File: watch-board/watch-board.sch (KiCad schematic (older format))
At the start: 60 parts

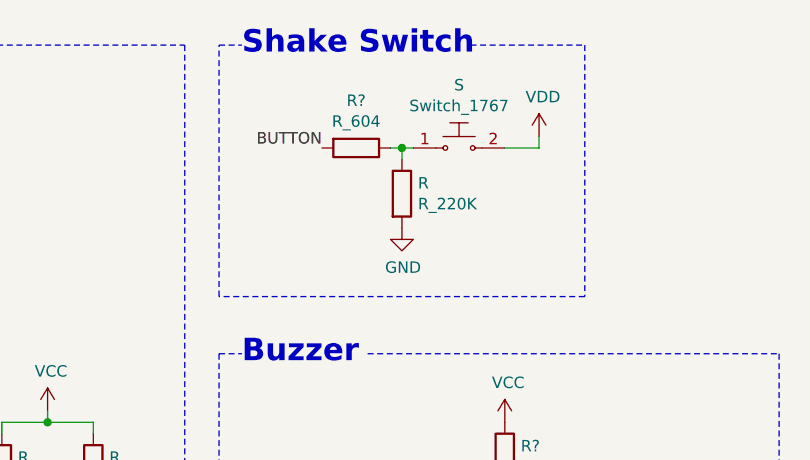
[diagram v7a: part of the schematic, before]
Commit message: Confirming shake-switch circuit -- adjusting pull-down and current limiting resistor
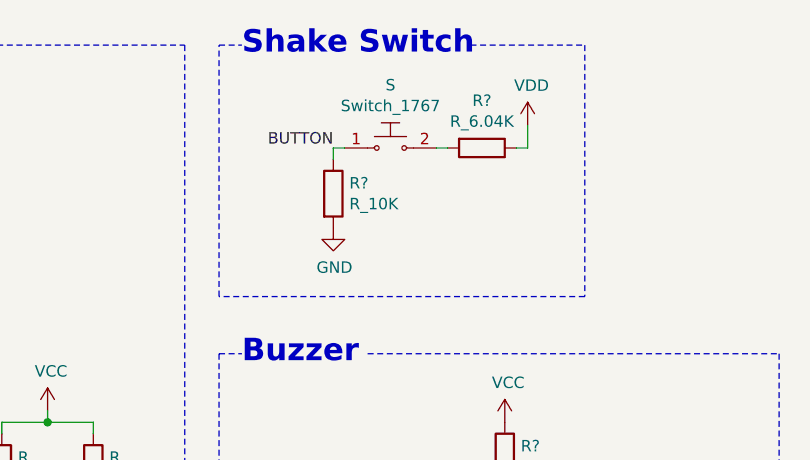
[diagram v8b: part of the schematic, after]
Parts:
- removed R: R_220K, Resistor_SMD:R_0805_2012Metric, symbol luke:R_220K
- removed R?: R_604, Resistor_SMD:R_0805_2012Metric, symbol luke:R_604
- added R?: R_6.04K, Resistor_SMD:R_0805_2012Metric, symbol luke:R_6.04K
- added R?: R_10K, Resistor_SMD:R_0805_2012Metric, symbol luke:R_10K
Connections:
- net BUTTON: now also S.1, R?.1
- net GND: now also R?.2
- net VDD: now also R?.1; no longer S.2
- new net: R?.2, S.2
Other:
- moved on the sheet: S
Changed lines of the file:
@@
 L luke:Switch_1767 S
 U 1 1 5F0E6B9E
-P 6850 1150
-F 0 "S" H 6850 1425 50  0000 C CNN
-F 1 "Switch_1767" H 6850 1334 50  0000 C CNN
-F 2 "Connector_PinSocket_2.54mm:PinSocket_1x02_P2.54mm_Vertical" H 7050 1350 50  0001 L CNN
-F 3 "https://media.digikey.com/pdf/Data%20Sheets/Adafruit%20PDFs/1767_Web.pdf" H 7050 1450 60  0001 L CNN
-F 4 "1528-2159-ND" H 7050 1550 60  0001 L CNN "Digi-Key_PN"
-F 5 "https://www.digikey.com/product-detail/en/adafruit-industries-llc/1767/1528-2159-ND/7244945" H 7050 1450 50  0001 L CNN "Purchasing Link"
-	1    6850 1150
-	1    0    0    -1
-$EndComp
-Text Label 6250 1150 2    50   ~ 0
+P 6550 1150
+F 0 "S" H 6550 1425 50  0000 C CNN
+F 1 "Switch_1767" H 6550 1334 50  0000 C CNN
+F 2 "Connector_PinSocket_2.54mm:PinSocket_1x02_P2.54mm_Vertical" H 6750 1350 50  0001 L CNN
+F 3 "https://media.digikey.com/pdf/Data%20Sheets/Adafruit%20PDFs/1767_Web.pdf" H 6750 1450 60  0001 L CNN
+F 4 "1528-2159-ND" H 6750 1550 60  0001 L CNN "Digi-Key_PN"
+F 5 "https://www.digikey.com/product-detail/en/adafruit-industries-llc/1767/1528-2159-ND/7244945" H 6750 1450 50  0001 L CNN "Purchasing Link"
+	1    6550 1150
+	1    0    0    -1
+$EndComp
+Text Label 6300 1150 2    50   ~ 0
 BUTTON
 Wire Wire Line
-	6550 1150 6600 1150
-$Comp
-L luke:R_220K R
-U 1 1 5ED88523
-P 6600 1350
-F 0 "R" H 6670 1396 50  0000 L CNN
-F 1 "R_220K" H 6670 1305 50  0000 L CNN
-F 2 "Resistor_SMD:R_0805_2012Metric" H 5500 1650 50  0001 L CNN
-F 3 "https://www.te.com/commerce/DocumentDelivery/DDEController?Action=srchrtrv&DocNm=1773204&DocType=DS&DocLang=English" H 5500 1750 50  0001 L CNN
-F 4 "A126350CT-ND" H 5500 1550 60  0001 L CNN "Digi-Key_PN"
-F 5 "https://www.digikey.com/product-detail/en/te-connectivity-passive-product/CRG0805F220K/A126350CT-ND/7603405" H 5500 1850 60  0001 L CNN "Purchasing Link"
-	1    6600 1350
-	1    0    0    -1
-$EndComp
-Wire Wire Line
-	6600 1200 6600 1150
-Connection ~ 6600 1150
-Wire Wire Line
-	6600 1150 6650 1150
+	6300 1200 6300 1150
 $Comp
 L power:GND #PWR
 U 1 1 5ED90D9E
-P 6600 1500
-F 0 "#PWR" H 6600 1250 50  0001 C CNN
-F 1 "GND" H 6605 1327 50  0000 C CNN
-F 2 "" H 6600 1500 50  0001 C CNN
-F 3 "" H 6600 1500 50  0001 C CNN
-	1    6600 1500
+P 6300 1500
+F 0 "#PWR" H 6300 1250 50  0001 C CNN
+F 1 "GND" H 6305 1327 50  0000 C CNN
+F 2 "" H 6300 1500 50  0001 C CNN
+F 3 "" H 6300 1500 50  0001 C CNN
+	1    6300 1500
 	1    0    0    -1
 $EndComp
@@
 L power:VDD #PWR
 U 1 1 5F1738F3
-P 7200 1100
-F 0 "#PWR" H 7200 950 50  0001 C CNN
-F 1 "VDD" H 7217 1273 50  0000 C CNN
-F 2 "" H 7200 1100 50  0001 C CNN
-F 3 "" H 7200 1100 50  0001 C CNN
-	1    7200 1100
-	1    0    0    -1
-$EndComp
-Wire Wire Line
-	7050 1150 7200 1150
-Wire Wire Line
-	7200 1150 7200 1100
+P 7150 1050
+F 0 "#PWR" H 7150 900 50  0001 C CNN
+F 1 "VDD" H 7167 1223 50  0000 C CNN
+F 2 "" H 7150 1050 50  0001 C CNN
+F 3 "" H 7150 1050 50  0001 C CNN
+	1    7150 1050
+	1    0    0    -1
+$EndComp
 Text Label 4850 5950 0    50   ~ 0
 VBAT_OK
@@
 	0    1    1    0
 $EndComp
-$Comp
-L luke:R_604 R?
-U 1 1 5FA72838
-P 6400 1150
-F 0 "R?" V 6193 1150 50  0000 C CNN
-F 1 "R_604" V 6284 1150 50  0000 C CNN
-F 2 "Resistor_SMD:R_0805_2012Metric" H 6330 1150 50  0001 C CNN
-F 3 "https://industrial.panasonic.com/cdbs/www-data/pdf/RDM0000/AOA0000C307.pdf" H 6480 1150 50  0001 C CNN
-F 4 "P604DACT-ND" H 6400 1150 60  0001 C CNN "Digi-Key_PN"
-F 5 "https://www.digikey.com/product-detail/en/panasonic-electronic-components/ERA-6AEB6040V/P604DACT-ND/3075200" H 6880 1550 60  0001 C CNN "Purchasing Link"
-	1    6400 1150
-	0    1    1    0
-$EndComp
 Text Notes 6500 6850 0    98   ~ 20
 Light
@@
 Wire Notes Line
 	5800 2050 5800 3850
+$Comp
+L luke:R_6.04K R?
+U 1 1 5F4C2EF6
+P 6950 1150
+F 0 "R?" V 6743 1150 50  0000 C CNN
+F 1 "R_6.04K" V 6834 1150 50  0000 C CNN
+F 2 "Resistor_SMD:R_0805_2012Metric" H 5850 1450 50  0001 L CNN
+F 3 "https://www.yageo.com/upload/media/product/productsearch/datasheet/rchip/PYu-RC_Group_51_RoHS_L_11.pdf" H 5850 1550 50  0001 L CNN
+F 4 "311-6.04KCRCT-ND" H 5850 1350 60  0001 L CNN "Digi-Key_PN"
+F 5 "https://www.digikey.com/product-detail/en/yageo/RC0805FR-076K04L/311-6-04KCRCT-ND/730996" H 5850 1650 60  0001 L CNN "Purchasing Link"
+	1    6950 1150
+	0    1    1    0
+$EndComp
+$Comp
+L luke:R_10K R?
+U 1 1 5F4F68AF
+P 6300 1350
+F 0 "R?" H 6370 1396 50  0000 L CNN
+F 1 "R_10K" H 6370 1305 50  0000 L CNN
+F 2 "Resistor_SMD:R_0805_2012Metric" H 5200 1650 50  0001 L CNN
+F 3 "https://www.yageo.com/upload/media/product/productsearch/datasheet/rchip/PYu-RC_Group_51_RoHS_L_10.pdf" H 5200 1750 50  0001 L CNN
+F 4 " 311-10.0KCRCT-ND " H 5200 1550 60  0001 L CNN "Digi-Key_PN"
+F 5 "https://www.digikey.com/product-detail/en/yageo/RC0805FR-0710KL/311-10-0KCRCT-ND/730482" H 5200 1850 60  0001 L CNN "Purchasing Link"
+	1    6300 1350
+	1    0    0    -1
+$EndComp
+Wire Wire Line
+	7150 1150 7100 1150
+Wire Wire Line
+	7150 1050 7150 1150
+Wire Wire Line
+	6800 1150 6750 1150
+Wire Wire Line
+	6350 1150 6300 1150
 $EndSCHEMATC
